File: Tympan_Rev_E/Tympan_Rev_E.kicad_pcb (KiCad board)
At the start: 2 copper layers, 82 parts, among them IC1 BC127, J1 SJ-3523-SMT-TR, J2 SJ-3524-SMT-TR-PI, P1 CONN_01X06, P2 CONN_01X06, P3 CONN_01X06, P4 CONN_01X06, P5 CONN_01X01, P6 CONN_01X01, P7 CONN_01X01, P8 CONN_01X01, SW1 CL-SB-22A, U1 MCP73831, U2 TLV320AIC3206IRSBT, U3 74LVC1G66, U4 LP5907MFX-1.8, U5 Teensy4.1

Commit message: draft layout of parts
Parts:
- F1, MIC1, MIC2, R2: moved to B.Cu
- U5: footprint teensy:Teensy41 -> teensy:Teensy41_SMT; moved to B.Cu
- moved BT2 219.8 mm to (275.1, 133.1), turned to 90 degrees
- moved SW1 214.8 mm to (223.7, 130.6), turned to 270 degrees
- moved F1 210.4 mm to (225.2, 129.6), turned to 270 degrees
- moved U5 209.8 mm to (240.0, 118.5), turned to 90 degrees
- moved J2 206.6 mm to (229.6, 78.4), turned to 270 degrees
- moved BT1 194.2 mm to (229.8, 142.5)
- moved D1 179.3 mm to (271.0, 143.0)
- moved J1 175.3 mm to (250.4, 78.4), turned to 270 degrees
- moved C17 174.7 mm to (256.5, 95.8), turned to 270 degrees
- moved R1 174.0 mm to (266.9, 140.1), turned to 180 degrees
- moved C23 173.4 mm to (265.4, 128.8)
- moved C20 172.7 mm to (255.5, 95.8), turned to 270 degrees
- moved U1 172.5 mm to (267.9, 142.4)
- moved R11 171.5 mm to (268.9, 140.1), turned to 180 degrees
- moved R12 171.3 mm to (271.0, 141.4)
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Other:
- board outline added: 38 x 74 mm

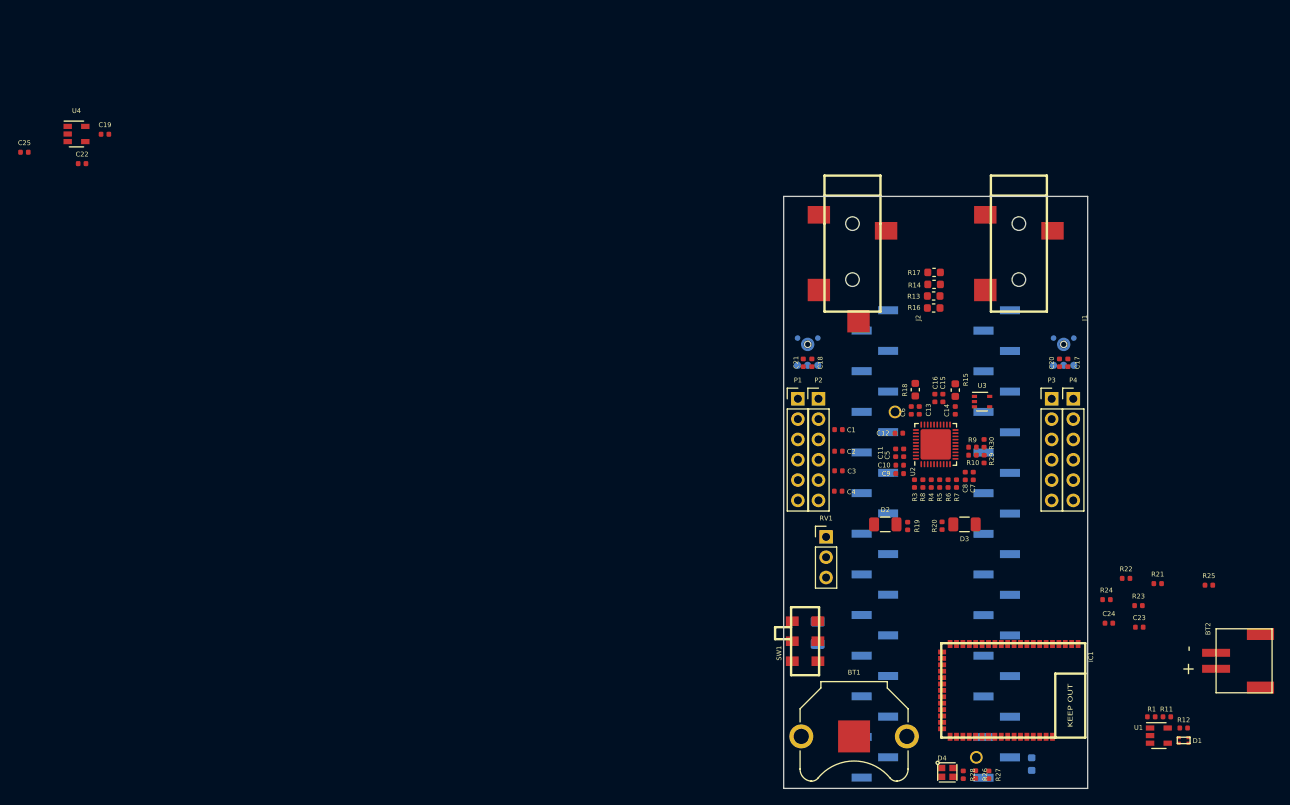
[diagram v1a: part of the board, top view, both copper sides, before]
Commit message: Component layout ready for routing
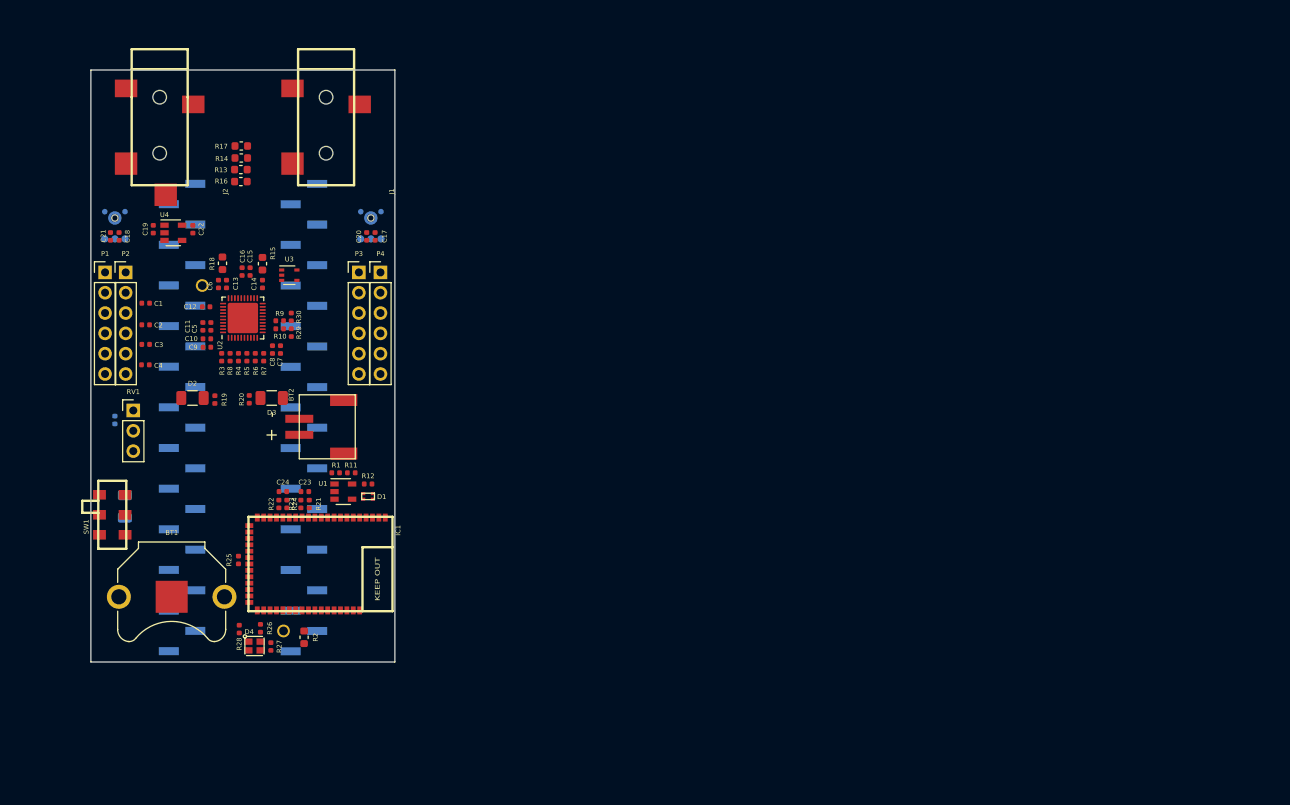
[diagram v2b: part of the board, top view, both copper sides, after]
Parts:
- C25: moved to B.Cu
- R2: moved to F.Cu
- moved R25 121.3 mm to (152.8, 120.5), turned to 90 degrees
- moved BT2 118.3 mm to (160.4, 103.8)
- moved R21 106.5 mm to (161.7, 113.5), turned to 270 degrees
- moved D1 106.4 mm to (169.1, 112.5)
- moved R1 106.4 mm to (165.0, 109.5)
- moved R11 106.4 mm to (166.9, 109.5)
- moved U1 106.4 mm to (165.9, 111.9)
- moved R12 106.4 mm to (169.1, 111.0)
- moved R22 106.3 mm to (157.9, 113.5), turned to 270 degrees
- moved C23 105.7 mm to (161.2, 111.9)
- moved R23 105.5 mm to (160.7, 113.5), turned to 90 degrees
- moved C24 104.6 mm to (158.4, 111.9)
- moved R24 103.1 mm to (158.9, 113.5), turned to 90 degrees
- moved R2 92.3 mm to (161.1, 130.1), turned to 270 degrees
- moved R28 92.3 mm to (152.9, 129.1)
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
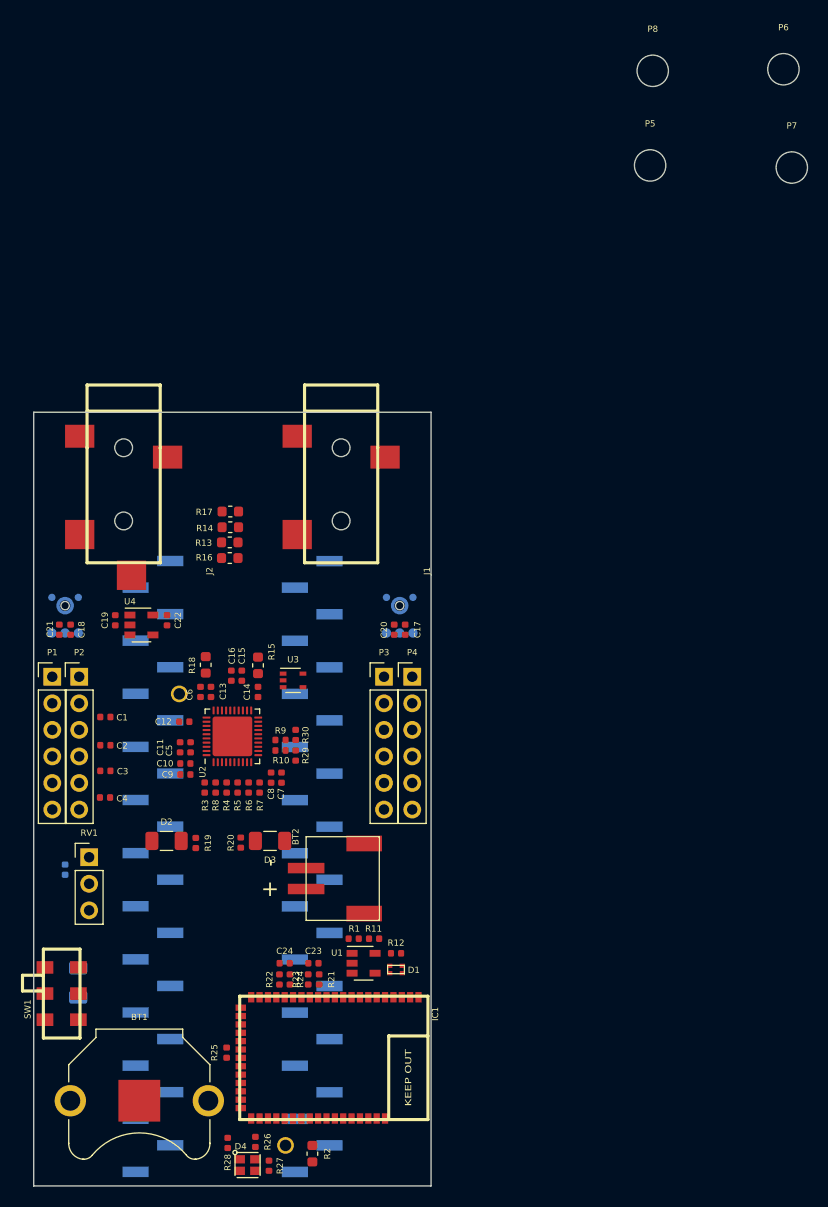
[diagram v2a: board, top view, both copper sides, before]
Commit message: Tracks Layout and Zone Fill
Passing DRC with minor courtyard flags. Needs touchup of tracks and silk.
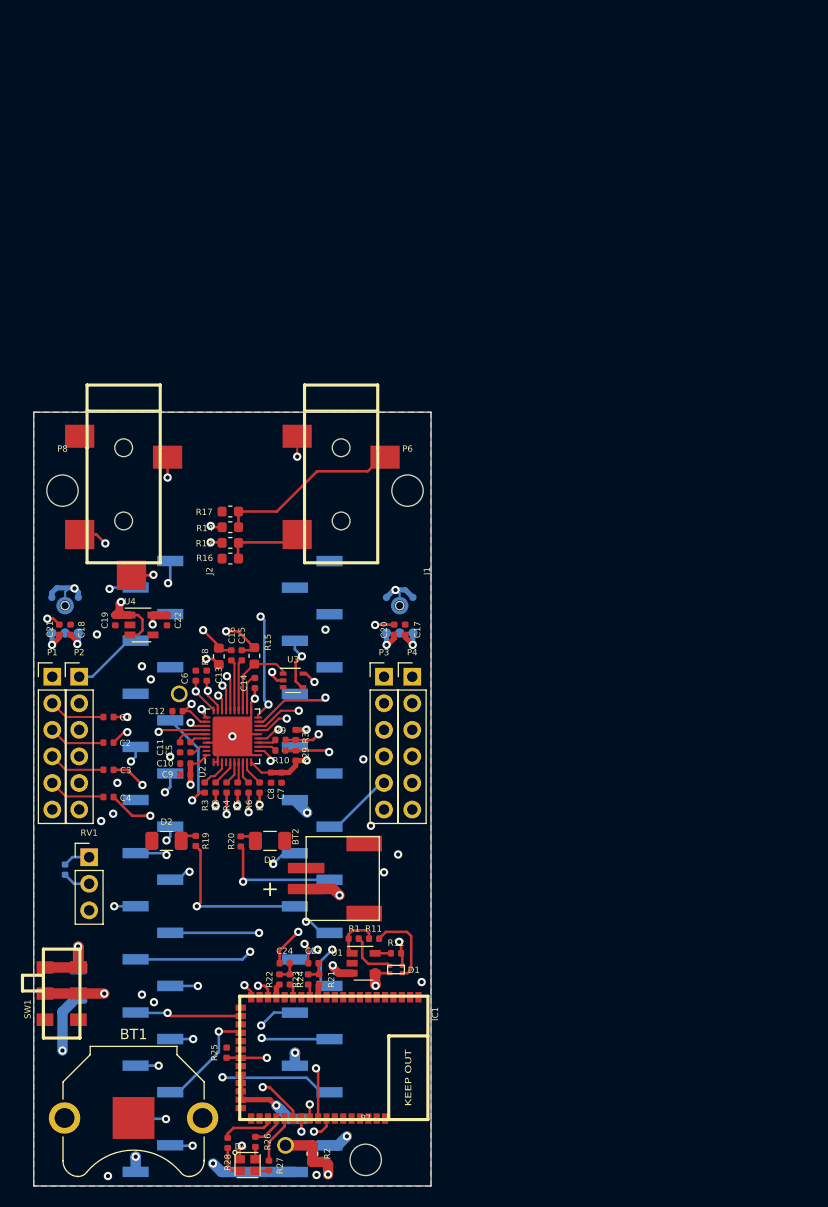
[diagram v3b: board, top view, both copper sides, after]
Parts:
- removed P5: CONN_01X01, MountingHole:MountingHole_3mm
- moved P7 103.3 mm to (166.2, 130.7)
- moved P8 69.3 mm to (137.2, 66.7)
- moved P6 54.0 mm to (170.2, 66.7)
- moved C15 1.95 mm to (154.3, 82.5)
- moved C16 1.95 mm to (153.3, 82.5)
- moved BT1 1.74 mm to (143.9, 126.7)
- moved C6 1.61 mm to (149.9, 84.4)
- moved C13 1.60 mm to (150.9, 84.4)
- moved R18 1.49 mm to (152.1, 82.5)
- moved C12 1.19 mm to (148.2, 87.8)
- moved R15 0.98 mm to (155.5, 82.5)
- moved C14 0.90 mm to (155.6, 85.1)
- moved C2 0.39 mm to (141.6, 90.8)
- moved C4 0.34 mm to (141.6, 96.0)
- moved C3 0.32 mm to (141.6, 93.4)
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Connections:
- BT1 pad 1: +BATT -> /V_BAT
- BT2 pad 3: (no net) -> GND
- BT2 pad 4: (no net) -> GND
- U5 pad 20: /BT_PIO5 -> Net-(U5-Pad20)
- U5 pad 21: /BT_PIO0 -> /M_BIAS_1
- U5 pad 22: /M_BIAS_1 -> Net-(U5-Pad22)
- U5 pad 25: /M_BIAS -> Net-(U5-Pad25)
- U5 pad 28: Net-(U5-Pad28) -> /M_BIAS
- U5 pad 37: /LED_R -> /LED_A
- U5 pad 38: /LED_A -> /LED_R
- U5 pad 4: Net-(U5-Pad4) -> /BT_PIO5
- U5 pad 44: /REV_TEST -> GND
- U5 pad 7: Net-(U5-Pad7) -> /BT_PIO0
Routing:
- net GND: track 0.00 -> 75.4 mm, vias 0 -> 11
- net /LOL: track 0.00 -> 58.3 mm, vias 0 -> 5
- net /MCLK: track 0.00 -> 58.3 mm, vias 0 -> 3
- net /LOR: track 0.00 -> 57.6 mm, vias 0 -> 5
- net /V_BAT: track 0.00 -> 55.9 mm
- net /BT_nRESET: track 0.00 -> 54.5 mm, vias 0 -> 4
- net /BCLK: track 0.00 -> 52.4 mm, vias 0 -> 3
- net /DOUT_1: track 0.00 -> 52.0 mm, vias 0 -> 2
- net /IN1_R: track 0.00 -> 49.3 mm, vias 0 -> 3
- net /WCLK: track 0.00 -> 48.9 mm, vias 0 -> 3
- net /IN1_L: track 0.00 -> 46.8 mm, vias 0 -> 3
- net /DIN_1: track 0.00 -> 43.2 mm, vias 0 -> 2
- net /MOSI: track 0.00 -> 35.1 mm, vias 0 -> 2
- net +BATT: track 0.00 -> 34.4 mm, vias 0 -> 3
- net +3V3: track 0.00 -> 33.6 mm, vias 0 -> 9
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- added copper zone on In1.Cu, net +1V8
- added copper zone on B.Cu, net +3V3
- added copper zone on In1.Cu, net +3V3
- added copper zone on In1.Cu, net +BATT
- added copper zone on In1.Cu, net /VIN
- added copper zone on F.Cu, net GND
- added copper zone on In2.Cu, net GND
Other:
- copper layers 2 -> 4

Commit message: updated silk
tidied up tracks and updated silk. Moved fuse from bottom to top, now only parts on bottom are teensy and microphones.
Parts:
- added G***: LOGO, Solutions:oshwa-logo-gear, B.Cu at (153.4, 64.2)
- added G***: LOGO, Solutions:Tympan_LOGO, F.Cu at (149.4, 107.3)
- C25, F1: moved to F.Cu
- moved C25 5.10 mm to (142.5, 103.0)
- moved F1 2.85 mm to (141.5, 113.7)
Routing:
- net +BATT: track 34.4 -> 37.5 mm
- net GND: track 75.4 -> 72.9 mm
- net /VIN: track 13.9 -> 12.4 mm
- net Net-(F1-Pad1): track 7.26 -> 6.03 mm, vias 1 -> 0
- net /DOUT_1: track 52.0 -> 50.8 mm
- net /POT: track 27.6 -> 28.5 mm
- net /MCLK: track 58.3 -> 58.8 mm
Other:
- board text added: "Designed by Flywheel Lab Brooklyn, NY"
- board text added: "Tympan Rev E"
- board text added: "www.tympan.org"

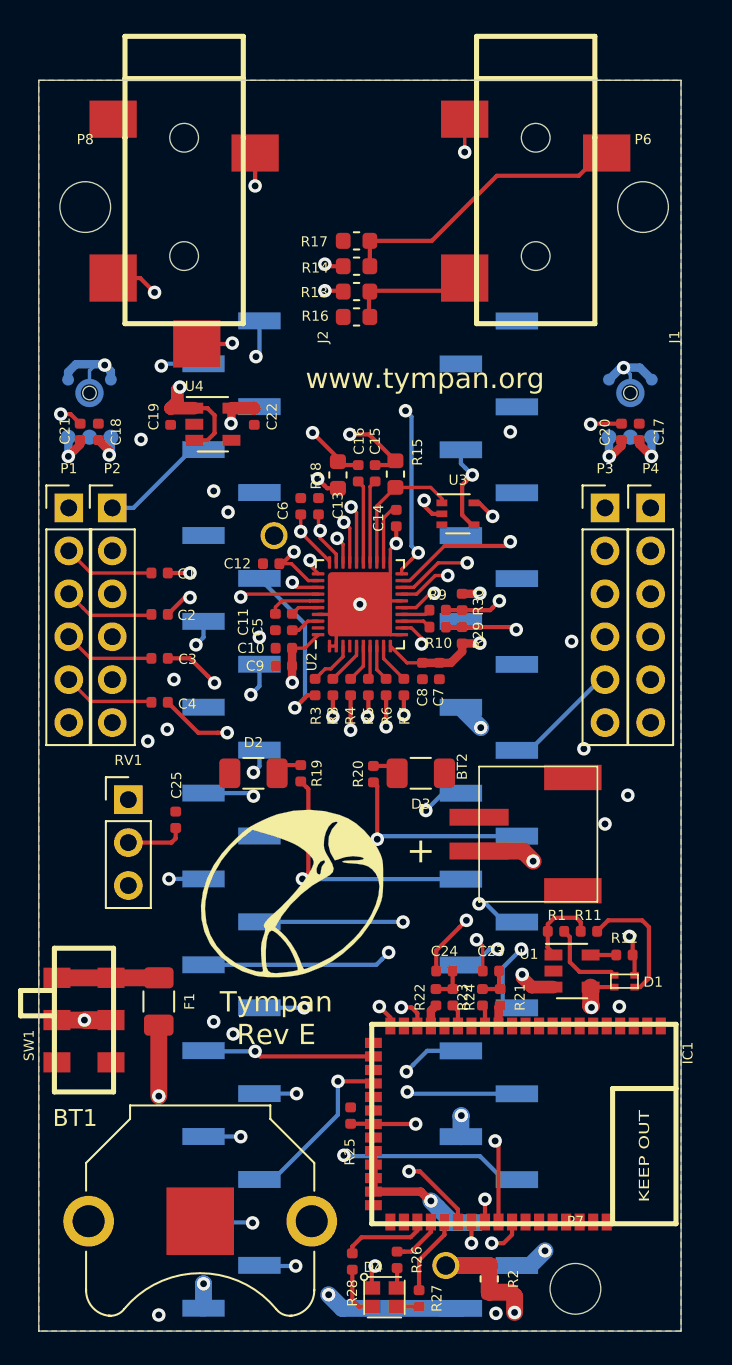
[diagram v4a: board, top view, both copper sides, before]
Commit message: Added pullup on BT reset pin and rout for battery cable
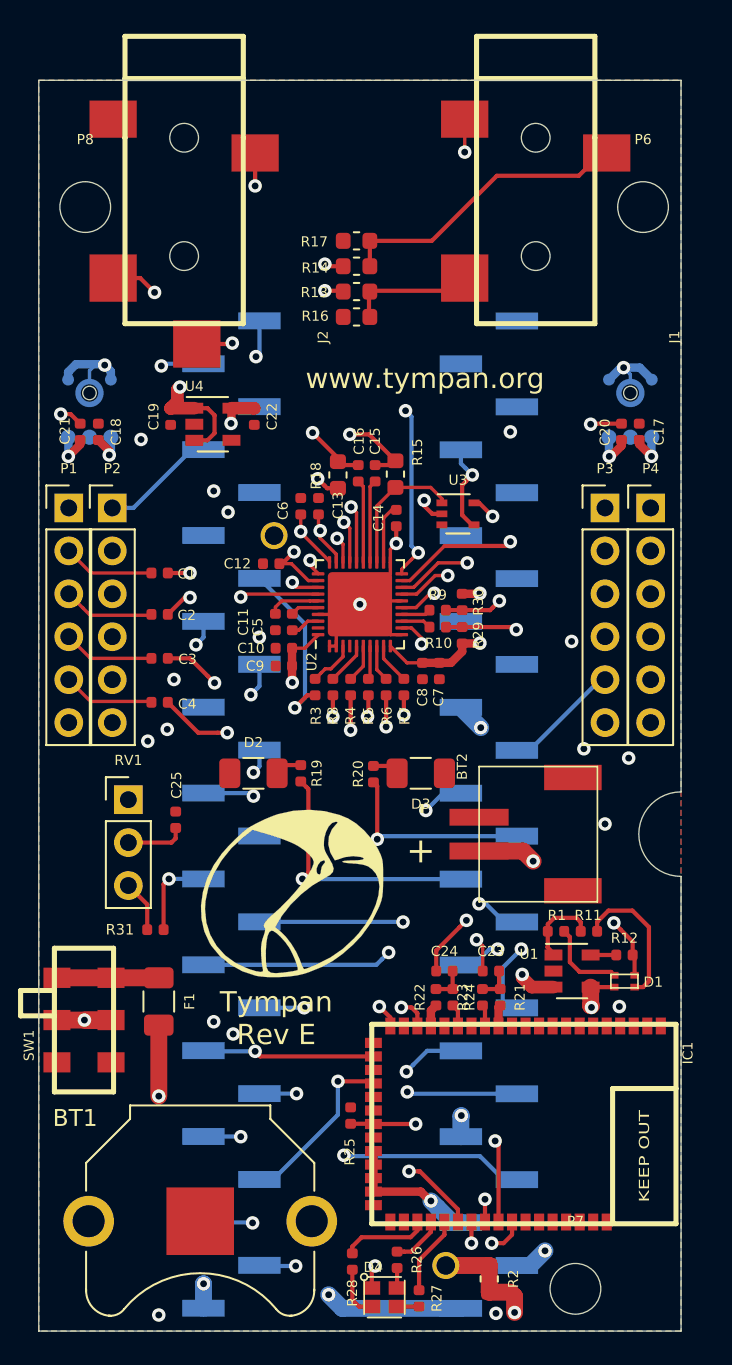
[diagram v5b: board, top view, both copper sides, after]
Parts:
- added R31: 10K, Resistor_SMD:R_0402_1005Metric, F.Cu at (141.3, 109.5)
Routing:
- net /BT_nRESET: track 54.8 -> 58.0 mm
- net +3V3: track 33.6 -> 36.7 mm
- net /MOSI: track 35.1 -> 33.9 mm
- net GND: track 72.9 -> 74.0 mm
- net Net-(D1-Pad4): track 7.59 -> 8.50 mm
- net /HPL: track 22.1 -> 21.6 mm
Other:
- outline, holes or cut-outs redrawn
